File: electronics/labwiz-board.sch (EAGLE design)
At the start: 93 parts, among them J1 SD_MICRO_SDIO_1BIT, J2 CORTEX_DEBUGSMD, J3 DNP, U1 STM32F10XRXT6, U2 MCP73831/2, U4 MIC5219-3.3V, X2 M12_BOTTOM_CONTACTS_FPC_1MM, Y3 32.768kHz

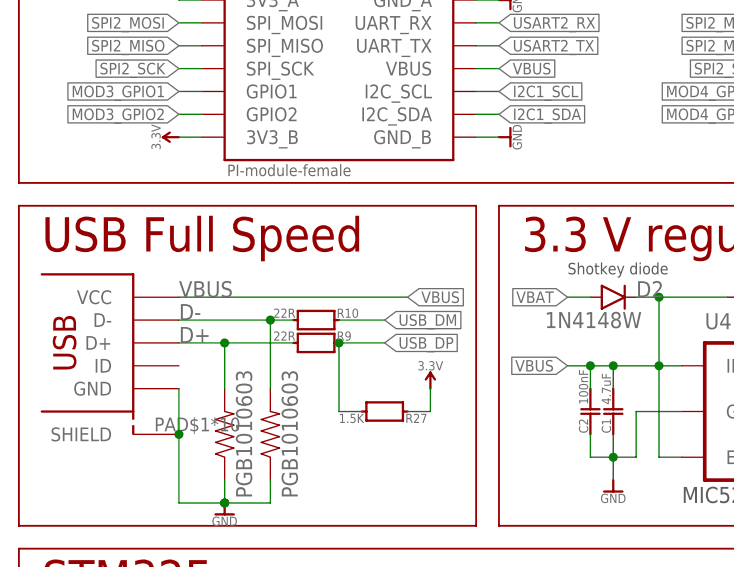
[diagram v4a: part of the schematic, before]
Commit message: Added a PTC fuse. #59.
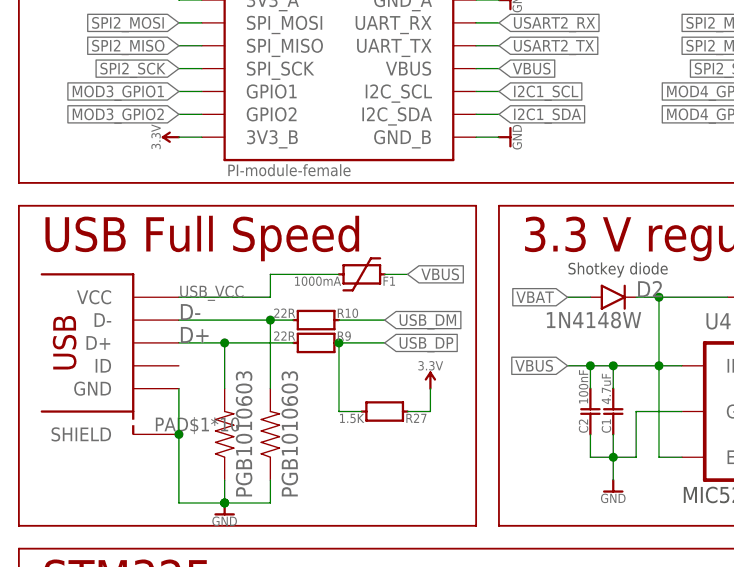
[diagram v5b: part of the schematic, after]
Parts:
- added F1: 1000mA, PaxInstruments-RCL:FUSE_RESETTABLE_PTC_1000MA_0805
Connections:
- new net USB_VCC: F1.1, U$1.VCC
- net VBUS: now also F1.2; no longer U$1.VCC
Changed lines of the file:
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@@
 <grid distance="0.1" unitdist="inch" unit="inch" style="lines" multiple="1" display="no" altdistance="0.01" altunitdist="inch" altunit="inch"/>
 <layers>
-<layer number="1" name="Top" color="4" fill="1" visible="no" active="no"/>
-<layer number="2" name="Route2" color="1" fill="3" visible="no" active="no"/>
-<layer number="3" name="Route3" color="4" fill="3" visible="no" active="no"/>
-<layer number="4" name="Route4" color="1" fill="4" visible="no" active="no"/>
-<layer number="5" name="Route5" color="4" fill="4" visible="no" active="no"/>
-<layer number="6" name="Route6" color="1" fill="8" visible="no" active="no"/>
-<layer number="7" name="Route7" color="4" fill="8" visible="no" active="no"/>
-<layer number="8" name="Route8" color="1" fill="2" visible="no" active="no"/>
-<layer number="9" name="Route9" color="4" fill="2" visible="no" active="no"/>
-<layer number="10" name="Route10" color="1" fill="7" visible="no" active="no"/>
-<layer number="11" name="Route11" color="4" fill="7" visible="no" active="no"/>
-<layer number="12" name="Route12" color="1" fill="5" visible="no" active="no"/>
-<layer number="13" name="Route13" color="4" fill="5" visible="no" active="no"/>
-<layer number="14" name="Route14" color="1" fill="6" visible="no" active="no"/>
-<layer number="15" name="Route15" color="4" fill="6" visible="no" active="no"/>
-<layer number="16" name="Bottom" color="1" fill="1" visible="no" active="no"/>
-<layer number="17" name="Pads" color="2" fill="1" visible="no" active="no"/>
-<layer number="18" name="Vias" color="2" fill="1" visible="no" active="no"/>
-<layer number="19" name="Unrouted" color="6" fill="1" visible="no" active="no"/>
-<layer number="20" name="Dimension" color="13" fill="1" visible="no" active="no"/>
-<layer number="21" name="tPlace" color="7" fill="1" visible="no" active="no"/>
-<layer number="22" name="bPlace" color="14" fill="1" visible="no" active="no"/>
-<layer number="23" name="tOrigins" color="15" fill="1" visible="no" active="no"/>
-<layer number="24" name="bOrigins" color="15" fill="1" visible="no" active="no"/>
-<layer number="25" name="tNames" color="7" fill="1" visible="no" active="no"/>
-<layer number="26" name="bNames" color="7" fill="1" visible="no" active="no"/>
-<layer number="27" name="tValues" color="7" fill="1" visible="no" active="no"/>
-<layer number="28" name="bValues" color="7" fill="1" visible="no" active="no"/>
+<layer number="1" name="Top" color="4" fill="1" visible="yes" active="no"/>
+<layer number="2" name="Route2" color="1" fill="3" visible="yes" active="no"/>
+<layer number="3" name="Route3" color="4" fill="3" visible="yes" active="no"/>
+<layer number="4" name="Route4" color="1" fill="4" visible="yes" active="no"/>
+<layer number="5" name="Route5" color="4" fill="4" visible="yes" active="no"/>
+<layer number="6" name="Route6" color="1" fill="8" visible="yes" active="no"/>
+<layer number="7" name="Route7" color="4" fill="8" visible="yes" active="no"/>
+<layer number="8" name="Route8" color="1" fill="2" visible="yes" active="no"/>
+<layer number="9" name="Route9" color="4" fill="2" visible="yes" active="no"/>
+<layer number="10" name="Route10" color="1" fill="7" visible="yes" active="no"/>
+<layer number="11" name="Route11" color="4" fill="7" visible="yes" active="no"/>
+<layer number="12" name="Route12" color="1" fill="5" visible="yes" active="no"/>
+<layer number="13" name="Route13" color="4" fill="5" visible="yes" active="no"/>
+<layer number="14" name="Route14" color="1" fill="6" visible="yes" active="no"/>
+<layer number="15" name="Route15" color="4" fill="6" visible="yes" active="no"/>
+<layer number="16" name="Bottom" color="1" fill="1" visible="yes" active="no"/>
+<layer number="17" name="Pads" color="2" fill="1" visible="yes" active="no"/>
+<layer number="18" name="Vias" color="2" fill="1" visible="yes" active="no"/>
+<layer number="19" name="Unrouted" color="6" fill="1" visible="yes" active="no"/>
+<layer number="20" name="Dimension" color="13" fill="1" visible="yes" active="no"/>
+<layer number="21" name="tPlace" color="7" fill="1" visible="yes" active="no"/>
+<layer number="22" name="bPlace" color="14" fill="1" visible="yes" active="no"/>
+<layer number="23" name="tOrigins" color="15" fill="1" visible="yes" active="no"/>
+<layer number="24" name="bOrigins" color="15" fill="1" visible="yes" active="no"/>
+<layer number="25" name="tNames" color="7" fill="1" visible="yes" active="no"/>
+<layer number="26" name="bNames" color="7" fill="1" visible="yes" active="no"/>
+<layer number="27" name="tValues" color="7" fill="1" visible="yes" active="no"/>
+<layer number="28" name="bValues" color="7" fill="1" visible="yes" active="no"/>
 <layer number="29" name="tStop" color="7" fill="3" visible="no" active="no"/>
 <layer number="30" name="bStop" color="7" fill="6" visible="no" active="no"/>
@@
 <layer number="35" name="tGlue" color="7" fill="4" visible="no" active="no"/>
 <layer number="36" name="bGlue" color="7" fill="5" visible="no" active="no"/>
-<layer number="37" name="tTest" color="7" fill="1" visible="no" active="no"/>
-<layer number="38" name="bTest" color="7" fill="1" visible="no" active="no"/>
+<layer number="37" name="tTest" color="7" fill="1" visible="yes" active="no"/>
+<layer number="38" name="bTest" color="7" fill="1" visible="yes" active="no"/>
 <layer number="39" name="tKeepout" color="4" fill="11" visible="no" active="no"/>
 <layer number="40" name="bKeepout" color="1" fill="11" visible="no" active="no"/>
@@
 <layer number="44" name="Drills" color="7" fill="1" visible="no" active="no"/>
 <layer number="45" name="Holes" color="7" fill="1" visible="no" active="no"/>
-<layer number="46" name="Milling" color="3" fill="1" visible="no" active="no"/>
-<layer number="47" name="Measures" color="7" fill="1" visible="no" active="no"/>
-<layer number="48" name="Document" color="7" fill="1" visible="no" active="no"/>
-<layer number="49" name="Reference" color="7" fill="1" visible="no" active="no"/>
-<layer number="50" name="dxf" color="7" fill="1" visible="no" active="no"/>
-<layer number="51" name="tDocu" color="6" fill="1" visible="no" active="no"/>
-<layer number="52" name="bDocu" color="7" fill="1" visible="no" active="no"/>
-<layer number="53" name="tGND_GNDA" color="7" fill="9" visible="no" active="no"/>
-<layer number="54" name="bGND_GNDA" color="1" fill="9" visible="no" active="no"/>
-<layer number="56" name="wert" color="7" fill="1" visible="no" active="no"/>
-<layer number="57" name="tCAD" color="7" fill="1" visible="no" active="no"/>
-<layer number="59" name="tCarbon" color="7" fill="1" visible="no" active="no"/>
-<layer number="60" name="bCarbon" color="7" fill="1" visible="no" active="no"/>
+<layer number="46" name="Milling" color="3" fill="1" visible="yes" active="no"/>
+<layer number="47" name="Measures" color="7" fill="1" visible="yes" active="no"/>
+<layer number="48" name="Document" color="7" fill="1" visible="yes" active="no"/>
+<layer number="49" name="Reference" color="7" fill="1" visible="yes" active="no"/>
+<layer number="50" name="dxf" color="7" fill="1" visible="yes" active="no"/>
+<layer number="51" name="tDocu" color="6" fill="1" visible="yes" active="no"/>
+<layer number="52" name="bDocu" color="7" fill="1" visible="yes" active="no"/>
+<layer number="53" name="tGND_GNDA" color="7" fill="9" visible="yes" active="no"/>
+<layer number="54" name="bGND_GNDA" color="1" fill="9" visible="yes" active="no"/>
+<layer number="56" name="wert" color="7" fill="1" visible="yes" active="no"/>
+<layer number="57" name="tCAD" color="7" fill="1" visible="yes" active="no"/>
+<layer number="59" name="tCarbon" color="7" fill="1" visible="yes" active="no"/>
+<layer number="60" name="bCarbon" color="7" fill="1" visible="yes" active="no"/>
 <layer number="90" name="Modules" color="5" fill="1" visible="yes" active="yes"/>
 <layer number="91" name="Nets" color="2" fill="1" visible="yes" active="yes"/>
@@
 <part name="TP9" library="PaxInstruments-Connectors" deviceset="M01" device="_PAD_1MM" value="DNP"/>
 <part name="TP10" library="PaxInstruments-Connectors" deviceset="M01" device="_PAD_1MM" value="DNP"/>
+<part name="F1" library="PaxInstruments-RCL" deviceset="FUSE_RESETTABLE_PTC" device="_0805" technology="_1000MA" value="1000mA"/>
 </parts>
 <sheets>
@@
 <instance part="TP9" gate="G$1" x="276.86" y="121.92"/>
 <instance part="TP10" gate="G$1" x="276.86" y="119.38"/>
+<instance part="F1" gate="G$1" x="43.18" y="185.42" rot="R90"/>
 </instances>
 <busses>
@@
 </segment>
 <segment>
-<pinref part="U$1" gate="G$1" pin="VCC"/>
-<label x="22.86" y="182.88" size="1.778" layer="95"/>
-<wire x1="22.86" y1="182.88" x2="48.26" y2="182.88" width="0.1524" layer="91"/>
-<label x="48.26" y="182.88" size="1.27" layer="95" xref="yes"/>
+<label x="48.26" y="185.42" size="1.27" layer="95" xref="yes"/>
+<wire x1="45.72" y1="185.42" x2="48.26" y2="185.42" width="0.1524" layer="91"/>
+<pinref part="F1" gate="G$1" pin="2"/>
 </segment>
 <segment>
@@
 </segment>
 </net>
+<net name="USB_VCC" class="0">
+<segment>
+<pinref part="U$1" gate="G$1" pin="VCC"/>
+<wire x1="22.86" y1="182.88" x2="33.02" y2="182.88" width="0.1524" layer="91"/>
+<wire x1="33.02" y1="182.88" x2="33.02" y2="185.42" width="0.1524" layer="91"/>
+<wire x1="33.02" y1="185.42" x2="40.64" y2="185.42" width="0.1524" layer="91"/>
+<label x="22.86" y="182.88" size="1.27" layer="95"/>
+<pinref part="F1" gate="G$1" pin="1"/>
+</segment>
+</net>

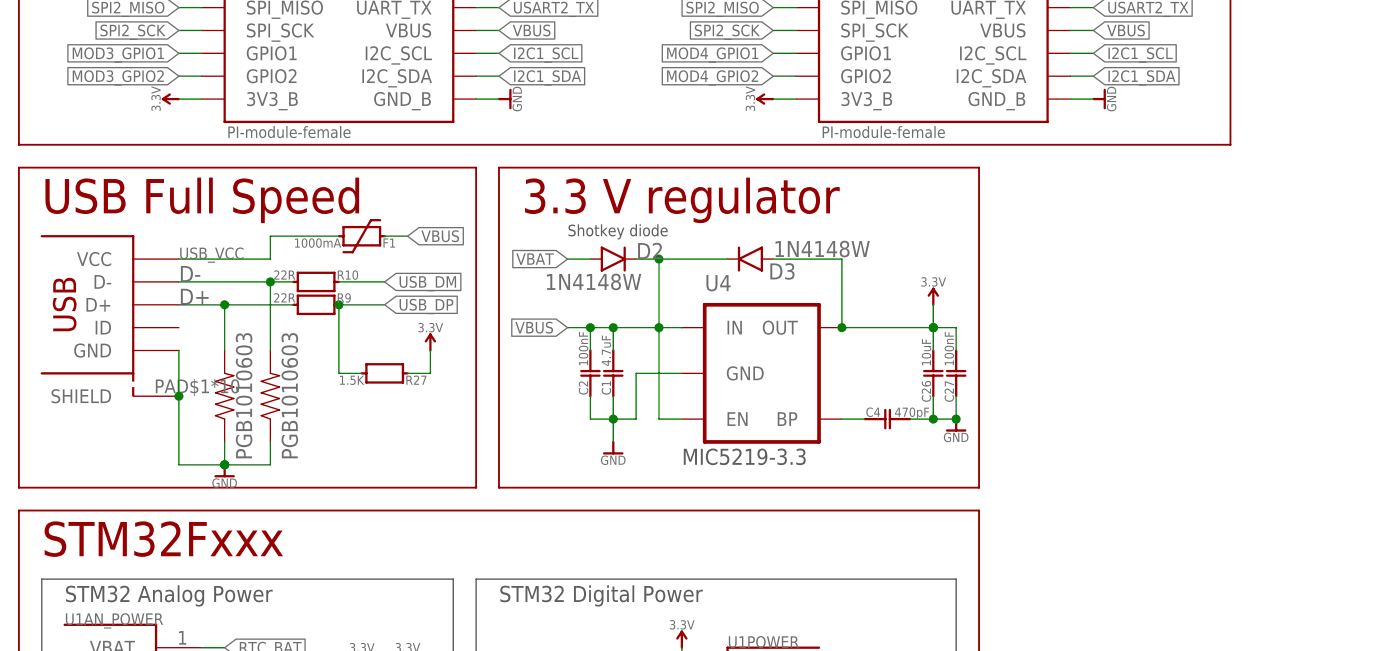
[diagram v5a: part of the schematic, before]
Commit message: Added transient voltage suppressor to USB_VCC. Closes #59.
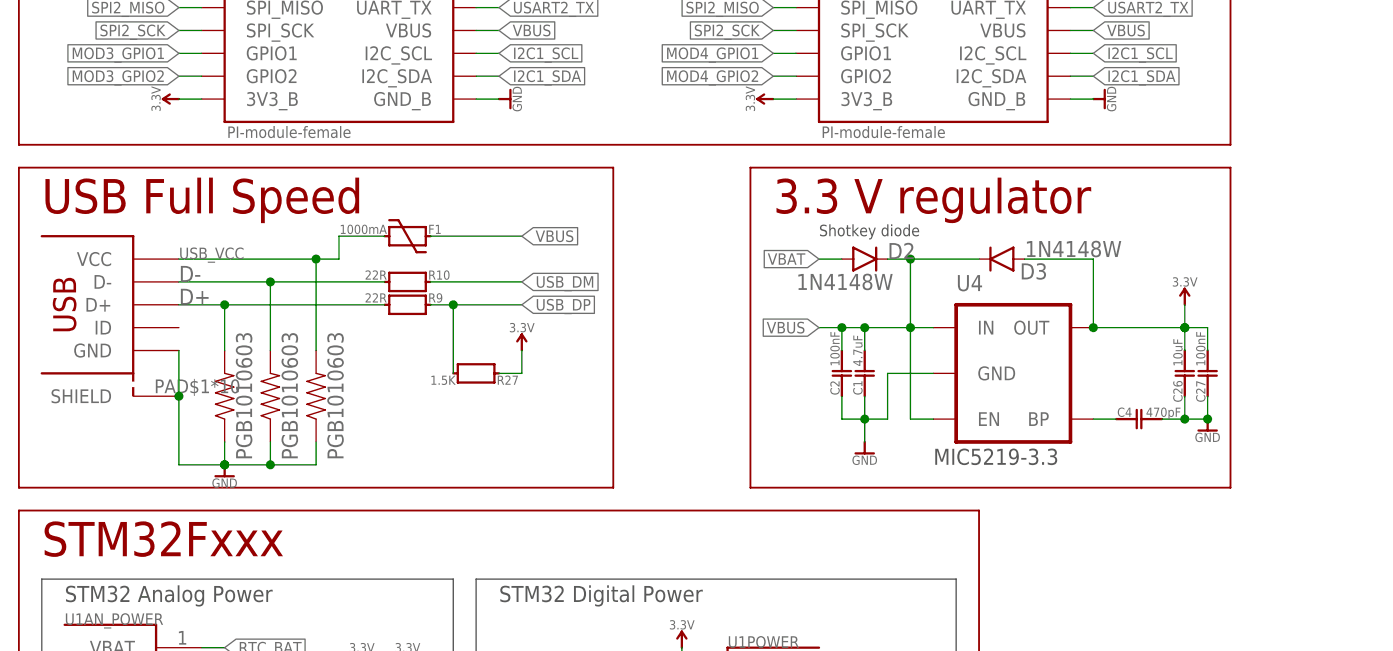
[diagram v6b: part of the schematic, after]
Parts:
- added Z3: PGB1010603, PaxInstrument-T400:SPARKFUN-RESISTORS_RESISTOR0603-RES
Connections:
- net GND: now also Z3.1
- net USB_VCC: now also Z3.2
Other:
- moved on the sheet: C1, C2, C26, C27, C4, D2, D3, F1, R10, R27, R9, U4

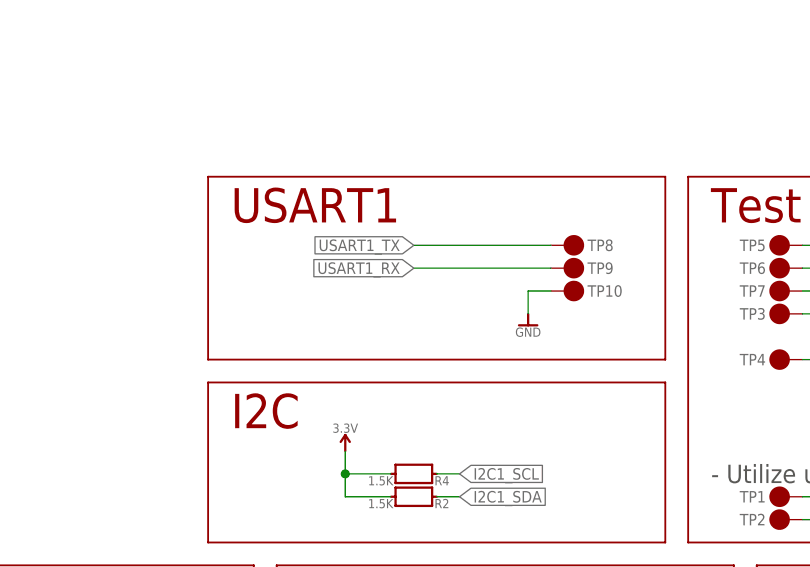
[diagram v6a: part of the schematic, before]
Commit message: Added 100k pullup resistors to the USART1 lines. Closes #26.
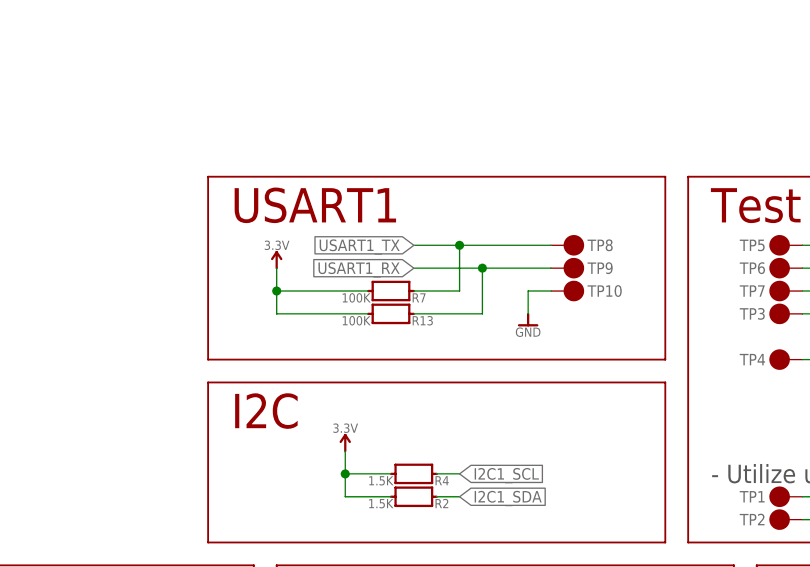
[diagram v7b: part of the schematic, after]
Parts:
- added R13, R7: 100K, PaxInstruments-RCL:RESISTOR_FIXED_100K_0402
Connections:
- net 3.3V: now also R13.1, R7.1
- net USART1_RX: now also R13.2
- net USART1_TX: now also R7.2
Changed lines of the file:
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@@
 <attribute name="MPN" value="PGB1010603NRHF"/>
 </part>
+<part name="R7" library="PaxInstruments-RCL" deviceset="RESISTOR_FIXED" device="_0402" technology="_100K" value="100K"/>
+<part name="R13" library="PaxInstruments-RCL" deviceset="RESISTOR_FIXED" device="_0402" technology="_100K" value="100K"/>
+<part name="SUPPLY5" library="PaxInstruments-Aesthetics" deviceset="SYM_VCC" device="" technology="3.3V" value="3.3V"/>
 </parts>
 <sheets>
@@
 <attribute name="MF" x="38.1" y="167.64" size="1.778" layer="96" rot="R90" display="off"/>
 </instance>
+<instance part="R7" gate="G$1" x="256.54" y="119.38" rot="R90"/>
+<instance part="R13" gate="G$1" x="256.54" y="116.84" rot="R90"/>
+<instance part="SUPPLY5" gate="G$1" x="243.84" y="121.92"/>
 </instances>
 <busses>
@@
 <junction x="251.46" y="99.06"/>
 </segment>
+<segment>
+<pinref part="R13" gate="G$1" pin="1"/>
+<pinref part="SUPPLY5" gate="G$1" pin="3.3V"/>
+<wire x1="254" y1="116.84" x2="243.84" y2="116.84" width="0.1524" layer="91"/>
+<wire x1="243.84" y1="116.84" x2="243.84" y2="119.38" width="0.1524" layer="91"/>
+<pinref part="R7" gate="G$1" pin="1"/>
+<wire x1="243.84" y1="119.38" x2="243.84" y2="121.92" width="0.1524" layer="91"/>
+<wire x1="254" y1="119.38" x2="243.84" y2="119.38" width="0.1524" layer="91"/>
+<junction x="243.84" y="119.38"/>
+</segment>
 </net>
 <net name="GND" class="5">
@@
 <segment>
 <label x="259.08" y="124.46" size="1.27" layer="95" rot="R180" xref="yes"/>
-<wire x1="259.08" y1="124.46" x2="274.32" y2="124.46" width="0.1524" layer="91"/>
+<wire x1="259.08" y1="124.46" x2="264.16" y2="124.46" width="0.1524" layer="91"/>
 <pinref part="TP8" gate="G$1" pin="P$1"/>
+<pinref part="R7" gate="G$1" pin="2"/>
+<wire x1="264.16" y1="124.46" x2="274.32" y2="124.46" width="0.1524" layer="91"/>
+<wire x1="259.08" y1="119.38" x2="264.16" y2="119.38" width="0.1524" layer="91"/>
+<wire x1="264.16" y1="119.38" x2="264.16" y2="124.46" width="0.1524" layer="91"/>
+<junction x="264.16" y="124.46"/>
 </segment>
 <segment>
@@
 <segment>
 <label x="259.08" y="121.92" size="1.27" layer="95" rot="R180" xref="yes"/>
-<wire x1="259.08" y1="121.92" x2="274.32" y2="121.92" width="0.1524" layer="91"/>
+<wire x1="259.08" y1="121.92" x2="266.7" y2="121.92" width="0.1524" layer="91"/>
 <pinref part="TP9" gate="G$1" pin="P$1"/>
-</segment>
-<segment>
+<pinref part="R13" gate="G$1" pin="2"/>
+<wire x1="266.7" y1="121.92" x2="274.32" y2="121.92" width="0.1524" layer="91"/>
+<wire x1="259.08" y1="116.84" x2="266.7" y2="116.84" width="0.1524" layer="91"/>
+<wire x1="266.7" y1="116.84" x2="266.7" y2="121.92" width="0.1524" layer="91"/>
+<junction x="266.7" y="121.92"/>
+</segment>
+<segment>
